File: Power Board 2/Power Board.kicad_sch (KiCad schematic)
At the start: 217 parts, among them IC1 LTC4151IMS#PBF, IC2 LTC4151IMS#PBF, J1 Conn_01x02, J10 Conn_01x02, J11 Conn_01x02, J12 Conn_01x02, J13 Conn_01x02, J14 Conn_01x02, J15 Conn_01x02, J16 Conn_01x02, J17 Conn_01x02, J18 Conn_02x03_Top_Bottom, J19 Conn_01x02, J2 Conn_01x02, J20 Conn_02x03_Top_Bottom, J21 Conn_01x02, J3 Conn_01x02, J4 Conn_01x02, J5 Conn_01x02, J6 Conn_01x02, J7 Conn_01x02, J8 Conn_01x02, J9 Conn_02x03_Top_Bottom, Q1 Q_PMOS_GDS, Q10 Q_NMOS_GDS, Q11 Q_NMOS_GDS, Q12 Q_NMOS_GDS, Q13 Q_NMOS_GDS, Q14 Q_NMOS_GDS, Q15 Q_NMOS_GDS, Q16 Q_NMOS_GDS, Q17 Q_NMOS_GDS, Q18 Q_NMOS_GDS, Q19 Q_NMOS_GDS, Q2 Q_PMOS_GDS, Q20 Q_NMOS_GDS, Q21 Q_NMOS_GDS, Q22 Q_NMOS_GDS, Q3 Q_PMOS_GDS, Q4 Q_PMOS_GDS, Q5 Q_PMOS_GDS, Q6 Q_PMOS_GDS, Q7 Q_PMOS_GDS, Q8 Q_PMOS_GDS, Q9 Q_NMOS_GDS, U1 LTC4372CDD-PBF, U10 ACS770xCB-050U-PFF, U11 ACS770xCB-050U-PFF, U12 ACS770xCB-050U-PFF, U13 ACS770xCB-050U-PFF, U14 ACS770xCB-050U-PFF, U15 ADC128S052CIMT, U16 ADC128S052CIMT, U17 TLV70033_SOT23-5, U2 LTC4372CDD-PBF, U3 LTC4372CDD-PBF, U4 LTC4372CDD-PBF, U5 LTC4372CDD-PBF, U6 LTC4372CDD-PBF, U7 LTC4372CDD-PBF, U8 ACS770xCB-050U-PFF, U9 ACS770xCB-050U-PFF

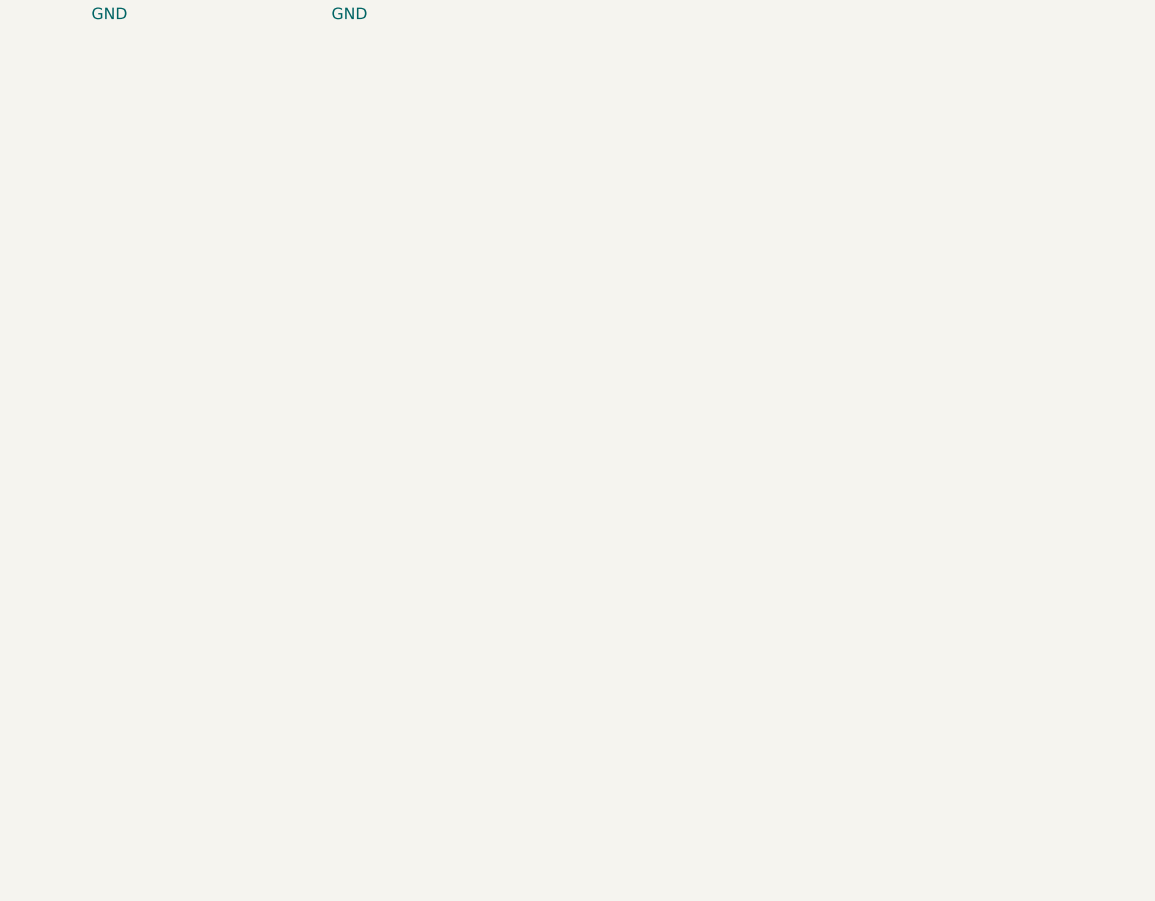
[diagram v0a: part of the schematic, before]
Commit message: pours and vias for battery outputs
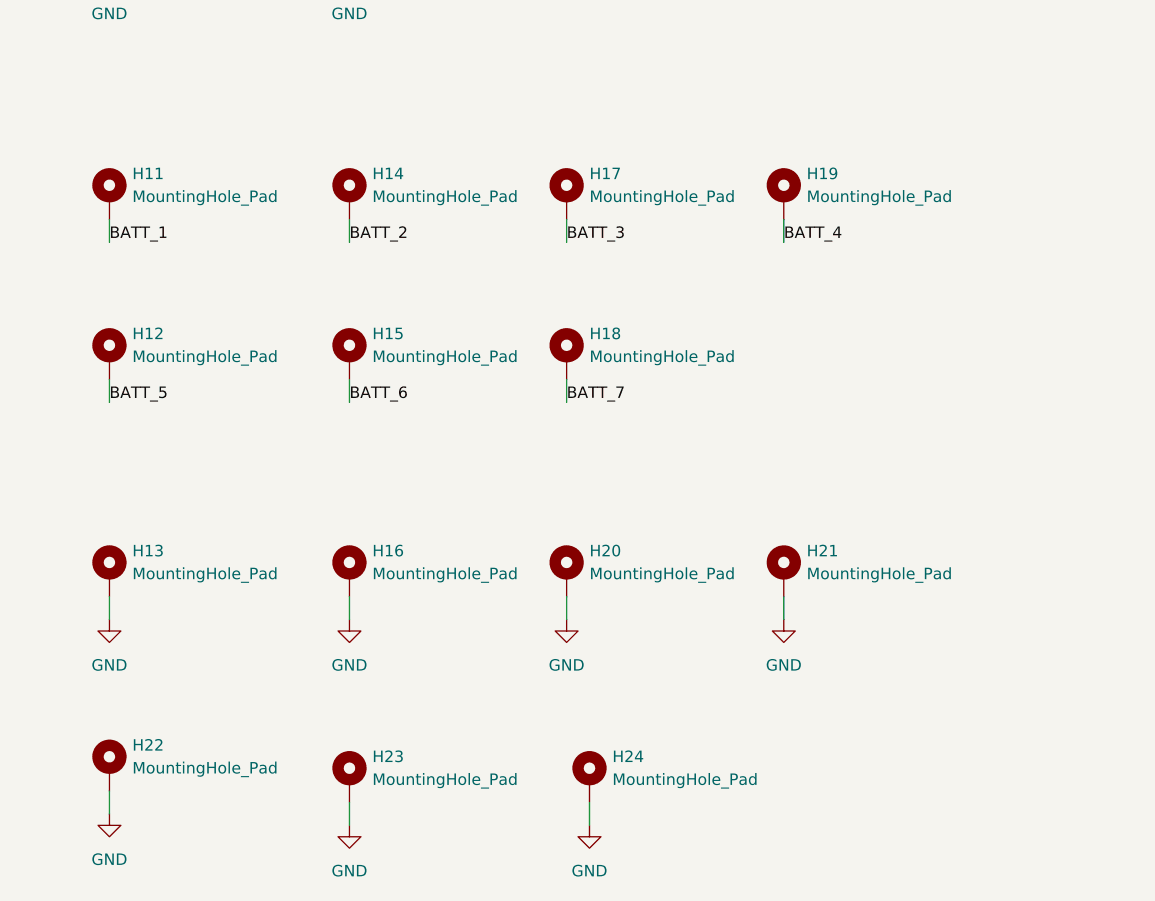
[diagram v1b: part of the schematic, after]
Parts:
- added H11, H12, H13, H14, H15, H16, H17, H18, H19, H20, H21, H22, H23, H24: MountingHole_Pad, MountingHole:MountingHole_4.3mm_M4_DIN965_Pad, symbol Mechanical:MountingHole_Pad
- H1, H10, H2, H3, H4, H5, H6, H7, H8, H9: footprint (none) -> MountingHole:MountingHole_3.2mm_M3_DIN965_Pad
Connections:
- net BATT_1: now also H11.1
- net BATT_2: now also H14.1
- net BATT_3: now also H17.1
- net BATT_4: now also H19.1
- net BATT_5: now also H12.1
- net BATT_6: now also H15.1
- net BATT_7: now also H18.1
- net GND: now also H13.1, H16.1, H20.1, H21.1, H22.1, H23.1, H24.1

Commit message: screw terminals for 5V buck, pour + stitching
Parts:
- removed C25, C26, C27, C28, C29, C30, C31, C53: 22 nF, Capacitor_SMD:C_0201_0603Metric_Pad0.64x0.40mm_HandSolder, symbol Device:C
- removed C32, C33: 0.1 uF, Capacitor_SMD:C_0201_0603Metric_Pad0.64x0.40mm_HandSolder, symbol Device:C
- removed C34: 1 uF, Capacitor_SMD:C_0201_0603Metric_Pad0.64x0.40mm_HandSolder, symbol Device:C
- removed J10, J11, J12, J13, J14, J15, J16, J17: Conn_01x02, Connector_Molex:Molex_KK-254_AE-6410-02A_1x02_P2.54mm_Vertical, symbol Connector_Generic:Conn_01x02
- removed J20: Conn_02x03_Top_Bottom, Connector_Molex:Molex_Nano-Fit_105314-xx06_2x03_P2.50mm_Horizontal, symbol Connector_Generic:Conn_02x03_Top_Bottom
- removed J_BMS1: Conn_01x04, symbol Connector_Generic:Conn_01x04
- removed J_BUS1: Conn_01x02, symbol Connector_Generic:Conn_01x02
- removed R34, R35, R36, R37: 33, Resistor_SMD:R_0805_2012Metric_Pad1.20x1.40mm_HandSolder, symbol Device:R
- removed RA10, RA11, RA12, RA13, RA14, RA15, RA8, RA9: 100, Resistor_SMD:R_0805_2012Metric_Pad1.20x1.40mm_HandSolder, symbol Device:R
- removed RT1, RT2, RT3, RT4, RT5, RT6, RT7, RT8: 2.7K, Resistor_SMD:R_0805_2012Metric_Pad1.20x1.40mm_HandSolder, symbol Device:R
- removed U16: ADC128S052CIMT, ADC128S052CIMT_NOPB:SOP65P640X120-16N, symbol ADC128S052CIMT:ADC128S052CIMT
- J19, J21: footprint (none) -> TerminalBlock_WAGO:TerminalBlock_WAGO_236-402_1x02_P5.00mm_45Degree
- J_I2C_Jetson1: footprint (none) -> Connector_Molex:Molex_Nano-Fit_105309-xx04_1x04_P2.50mm_Vertical
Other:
- note removed: "Thermistor"
- note removed: "Thermistor ADC"

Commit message: changed mounting holes to without pad for star grounding
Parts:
- added H25, H26, H27, H28: MountingHole_Pad, MountingHole:MountingHole_3.2mm_M3_DIN965_Pad, symbol Mechanical:MountingHole_Pad
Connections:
- net GND: now also H25.1, H26.1, H27.1, H28.1

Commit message: power board minor changes
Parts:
- C1, C10, C11, C12, C13, C14, C15, C16, C17, C18, C19, C2, C20, C21, C22, C23, C24, C3, C35, C36, C37, C38, C39, C4, C40, C41, C42, C43, C44, C45, C46, C47, C48, C49, C5, C50, C6, C7, C8, C9: footprint Capacitor_SMD:C_0201_0603Metric_Pad0.64x0.40mm_HandSolder -> Capacitor_SMD:C_0603_1608Metric
- C54: footprint Capacitor_SMD:C_0805_2012Metric_Pad1.18x1.45mm_HandSolder -> Capacitor_SMD:C_0805_2012Metric
- H1, H10, H2, H25, H26, H27, H28, H3, H4, H5, H6, H7, H8, H9: footprint MountingHole:MountingHole_3.2mm_M3_DIN965_Pad -> MountingHole:MountingHole_3.2mm_M3_DIN965; symbol Mechanical:MountingHole_Pad -> Mechanical:MountingHole
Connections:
- net GND: no longer H1.1, H10.1, H2.1, H25.1, H26.1, H27.1, H28.1, H3.1, H4.1, H5.1, H6.1, H7.1, H8.1, H9.1

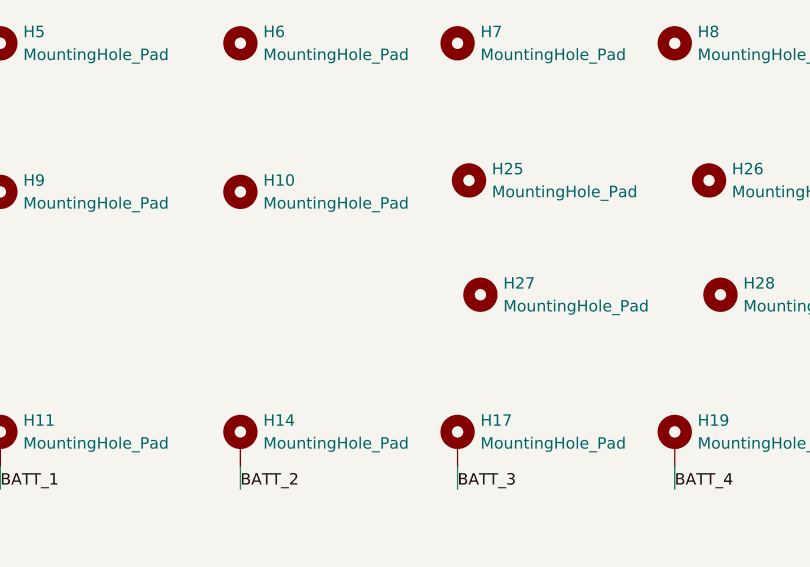
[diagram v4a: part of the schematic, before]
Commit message: added mounting holes
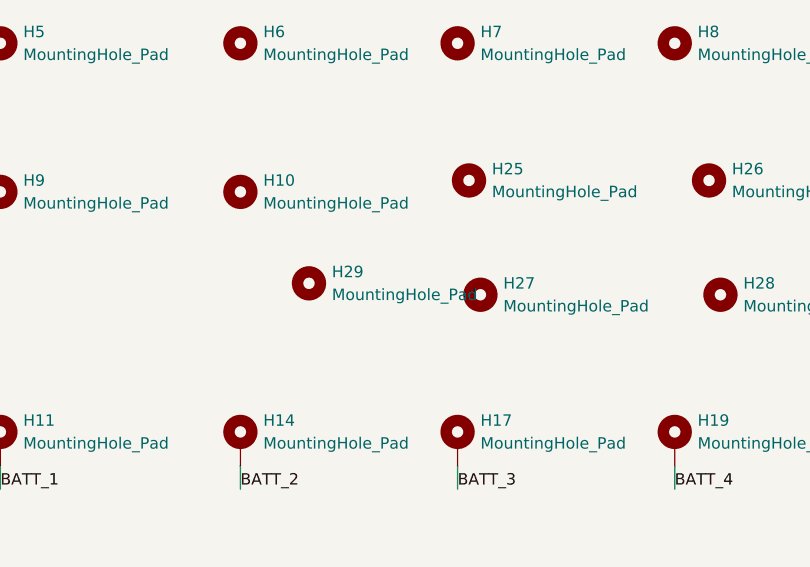
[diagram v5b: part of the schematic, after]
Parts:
- added H29: MountingHole_Pad, MountingHole:MountingHole_3.2mm_M3_DIN965, symbol Mechanical:MountingHole
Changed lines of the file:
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@@
+	)
+	(symbol
+		(lib_id "Mechanical:MountingHole")
+		(at 60.96 367.03 0)
+		(unit 1)
+		(exclude_from_sim no)
+		(in_bom no)
+		(on_board yes)
+		(dnp no)
+		(fields_autoplaced yes)
+		(property "Reference" "H29"
+			(at 63.5 365.7599 0)
+			(effects
+				(font
+					(size 1.27 1.27)
+				)
+				(justify left)
+			)
+		)
+		(property "Value" "MountingHole_Pad"
+			(at 63.5 368.2999 0)
+			(effects
+				(font
+					(size 1.27 1.27)
+				)
+				(justify left)
+			)
+		)
+		(property "Footprint" "MountingHole:MountingHole_3.2mm_M3_DIN965"
+			(at 60.96 367.03 0)
+			(effects
+				(font
+					(size 1.27 1.27)
+				)
+				(hide yes)
+			)
+		)
+		(property "Datasheet" "~"
+			(at 60.96 367.03 0)
+			(effects
+				(font
+					(size 1.27 1.27)
+				)
+				(hide yes)
+			)
+		)
+		(property "Description" "Mounting Hole without connection"
+			(at 60.96 367.03 0)
+			(effects
+				(font
+					(size 1.27 1.27)
+				)
+				(hide yes)
+			)
+		)
+		(instances
+			(project "Power Board"
+				(path "/52f7cba9-f573-43e9-b6c5-44859a4c1733"
+					(reference "H29")
+					(unit 1)
+				)
+			)
+		)
 	)
 	(symbol
